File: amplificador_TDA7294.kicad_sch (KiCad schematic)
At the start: 13 parts, among them U1 TDA7294

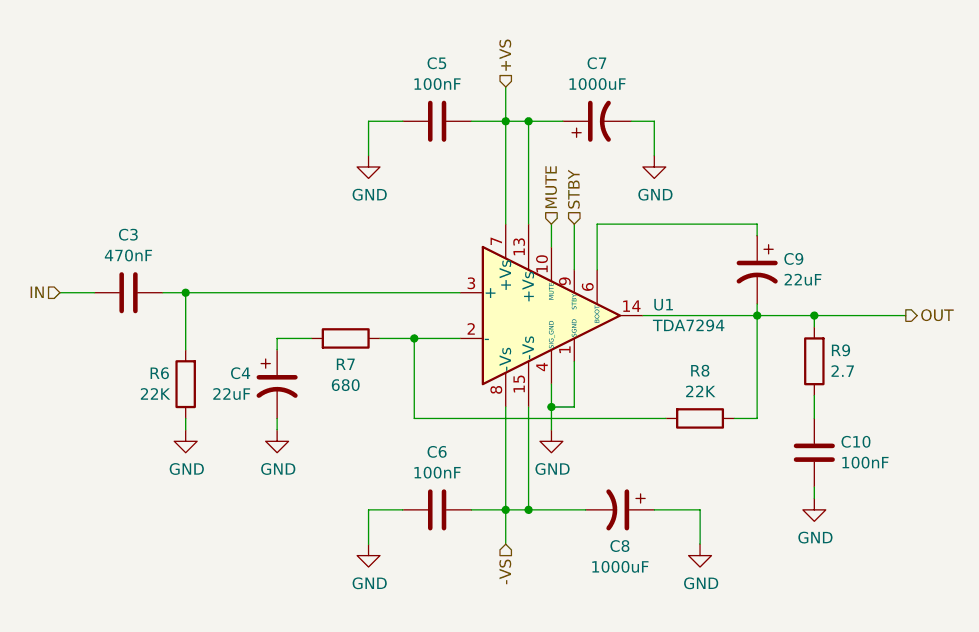
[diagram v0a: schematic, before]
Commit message: eliminando archivos extras
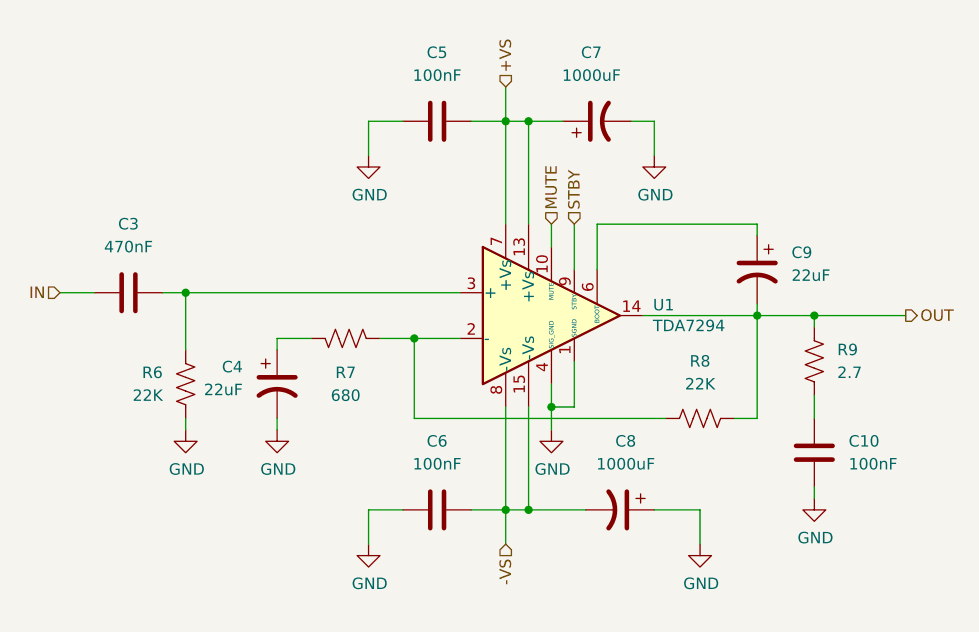
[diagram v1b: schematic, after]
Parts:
- C4, C7, C8, C9: symbol TDA7294-rescue:CP1-Device -> Device:C_Polarized_US
- R6, R7, R8, R9: symbol Device:R -> Device:R_US

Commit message: completada version 1.1.0 con TDA al mismo lado
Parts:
- C7, C8: footprint Capacitor_THT:CP_Radial_D13.0mm_P5.00mm -> Capacitor_THT:CP_Radial_D10.0mm_P5.00mm; VOLTAGE (none) -> 35V
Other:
- company: (none) -> MAYKOLREY.COM
- title: (none) -> Amplificador TDA7294
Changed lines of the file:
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@@
 (kicad_sch (version 20230121) (generator eeschema)
   (paper "A4")
+  (title_block
+    (title "Amplificador TDA7294")
+    (date "2023-12-17")
+    (rev "v1.1.0")
+    (company "MAYKOLREY.COM")
+  )
   (junction (at 144.78 118.11) (diameter 0) (color 0 0 0 0)
   )
@@
   (symbol (lib_id "Device:C_Polarized_US") (at 157.48 118.11 270) (unit 1)
     (in_bom yes) (on_board yes) (dnp no) (fields_autoplaced)
-    (property "Reference" "C8" (at 158.115 110.49 90)
-      (effects (font (size 1.27 1.27)))
-    )
-    (property "Value" "1000uF" (at 158.115 113.03 90)
-      (effects (font (size 1.27 1.27)))
-    )
-    (property "Footprint" "Capacitor_THT:CP_Radial_D13.0mm_P5.00mm" (at 157.48 118.11 0)
+    (property "Reference" "C8" (at 158.115 123.19 90)
+      (effects (font (size 1.27 1.27)))
+    )
+    (property "Value" "1000uF" (at 158.115 125.73 90)
+      (effects (font (size 1.27 1.27)))
+    )
+    (property "Footprint" "Capacitor_THT:CP_Radial_D10.0mm_P5.00mm" (at 157.48 118.11 0)
       (effects (font (size 1.27 1.27)) hide)
     )
     (property "Datasheet" "~" (at 157.48 118.11 0)
       (effects (font (size 1.27 1.27)) hide)
+    )
+    (property "LCSC Part" "" (at 157.48 118.11 0)
+      (effects (font (size 1.27 1.27)) hide)
+    )
+    (property "Mfr. Part" "" (at 157.48 118.11 0)
+      (effects (font (size 1.27 1.27)) hide)
+    )
+    (property "Manufacturer" "" (at 157.48 118.11 0)
+      (effects (font (size 1.27 1.27)) hide)
+    )
+    (property "Description" "" (at 157.48 118.11 0)
+      (effects (font (size 1.27 1.27)) hide)
+    )
+    (property "Price" "" (at 157.48 118.11 0)
+      (effects (font (size 1.27 1.27)) hide)
+    )
+    (property "VOLTAGE" "35V" (at 158.115 128.27 90)
+      (effects (font (size 1.27 1.27)))
     )
     (pin "1")
@@
   (symbol (lib_id "Device:C_Polarized_US") (at 154.94 74.93 90) (unit 1)
     (in_bom yes) (on_board yes) (dnp no) (fields_autoplaced)
-    (property "Reference" "C7" (at 154.305 67.31 90)
-      (effects (font (size 1.27 1.27)))
-    )
-    (property "Value" "1000uF" (at 154.305 69.85 90)
-      (effects (font (size 1.27 1.27)))
-    )
-    (property "Footprint" "Capacitor_THT:CP_Radial_D13.0mm_P5.00mm" (at 154.94 74.93 0)
+    (property "Reference" "C7" (at 154.305 64.77 90)
+      (effects (font (size 1.27 1.27)))
+    )
+    (property "Value" "1000uF" (at 154.305 67.31 90)
+      (effects (font (size 1.27 1.27)))
+    )
+    (property "Footprint" "Capacitor_THT:CP_Radial_D10.0mm_P5.00mm" (at 154.94 74.93 0)
       (effects (font (size 1.27 1.27)) hide)
     )
@@
       (effects (font (size 1.27 1.27)) hide)
     )
-    (pin "1")
+    (property "LCSC Part" "" (at 154.94 74.93 0)
+      (effects (font (size 1.27 1.27)) hide)
+    )
+    (property "Mfr. Part" "" (at 154.94 74.93 0)
+      (effects (font (size 1.27 1.27)) hide)
+    )
+    (property "Manufacturer" "" (at 154.94 74.93 0)
+      (effects (font (size 1.27 1.27)) hide)
+    )
+    (property "Description" "" (at 154.94 74.93 0)
+      (effects (font (size 1.27 1.27)) hide)
+    )
+    (property "Price" "" (at 154.94 74.93 0)
+      (effects (font (size 1.27 1.27)) hide)
+    )
+    (property "VOLTAGE" "35V" (at 154.305 69.85 90)
+      (effects (font (size 1.27 1.27)))
+    )
+    (pin "1")

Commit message: mejorando los conectores
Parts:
- C10, C5, C6: footprint Capacitor_THT:C_Disc_D4.3mm_W1.9mm_P5.00mm -> Capacitor_THT:C_Disc_D4.7mm_W2.5mm_P5.00mm; LCSC Part (none) -> C254094; Manufacturer (none) -> Dersonic; Mfr. Part (none) -> CC1H104ZC74D3F5O30MN; Price (none) -> 0.0158; VOLTAGE (none) -> 50V
- C7, C8: LCSC Part (none) -> C398835; Manufacturer (none) -> AISHI(Aihua Group); Mfr. Part (none) -> ERR1VM102G20OT; Price (none) -> 0.1211
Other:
- moved on the sheet: C10
